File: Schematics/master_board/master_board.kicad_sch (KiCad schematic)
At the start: 48 parts, among them J1 2x5x1.27mm, J2 USB_C_Receptacle_USB2.0, J3 Conn_01x01_Female, J4 Conn_01x01_Female, J5 Conn_01x01_Female, J6 Conn_01x01_Female, SW1 SW_Push, SW2 SW_Push, SW3 SW_Push, U1 NCP1117-3.3_SOT223, U2 RP2040, U3 W25Q16JVSSIQ, Y1 ABLS-12.000MHZ-B4-T

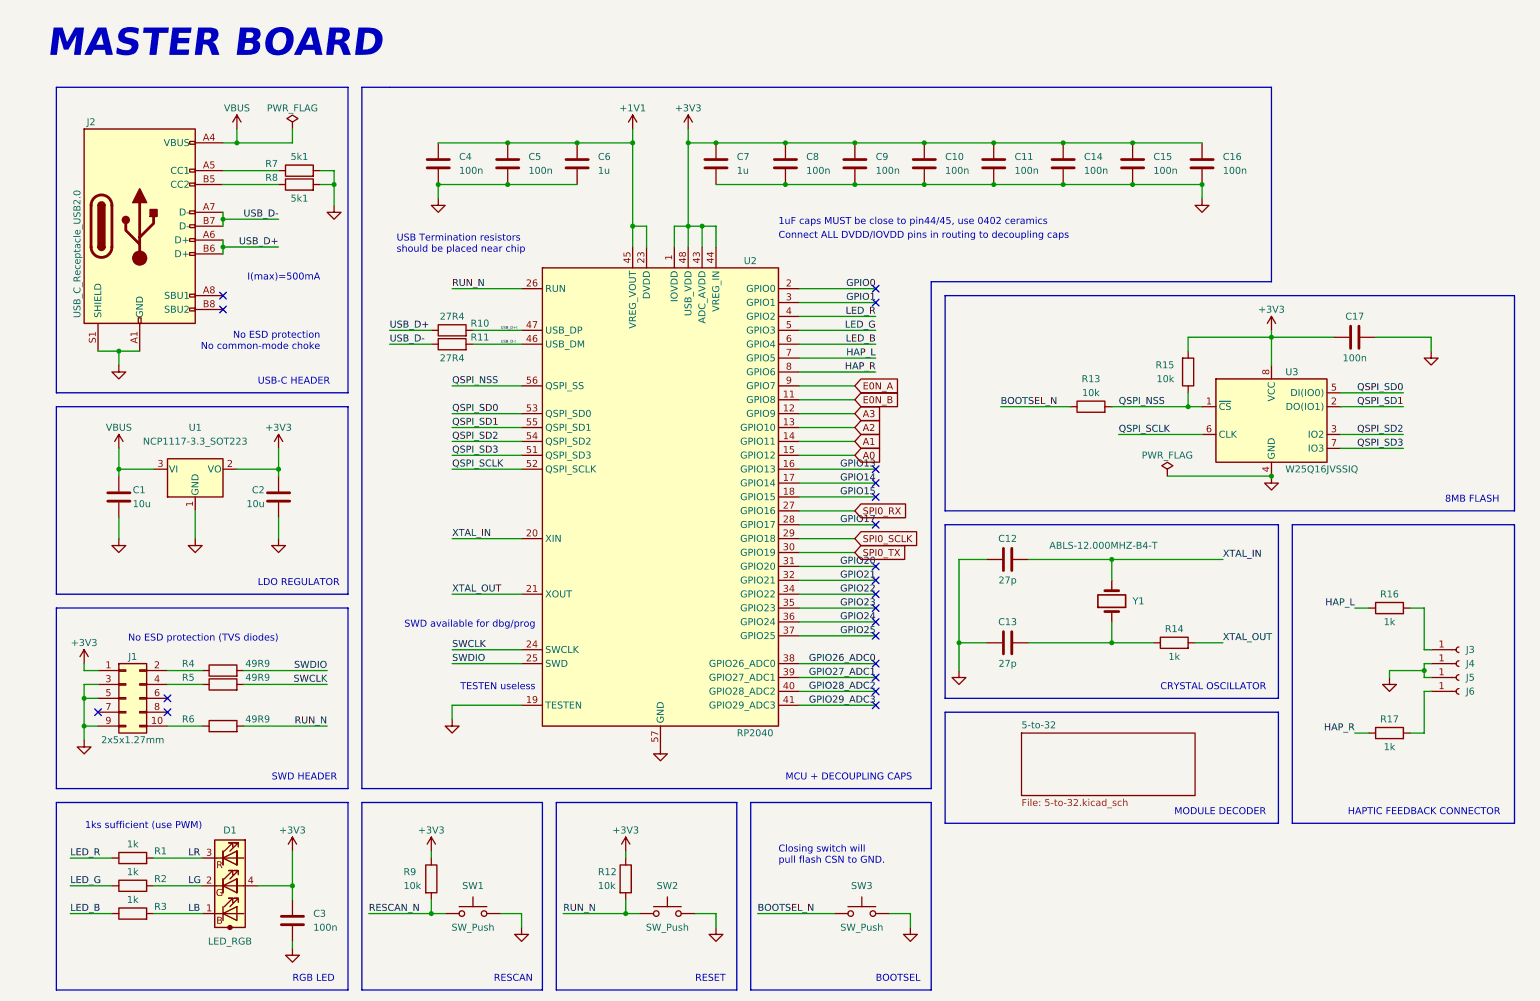
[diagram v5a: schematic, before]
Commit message: Finalize master board placement, begin routing
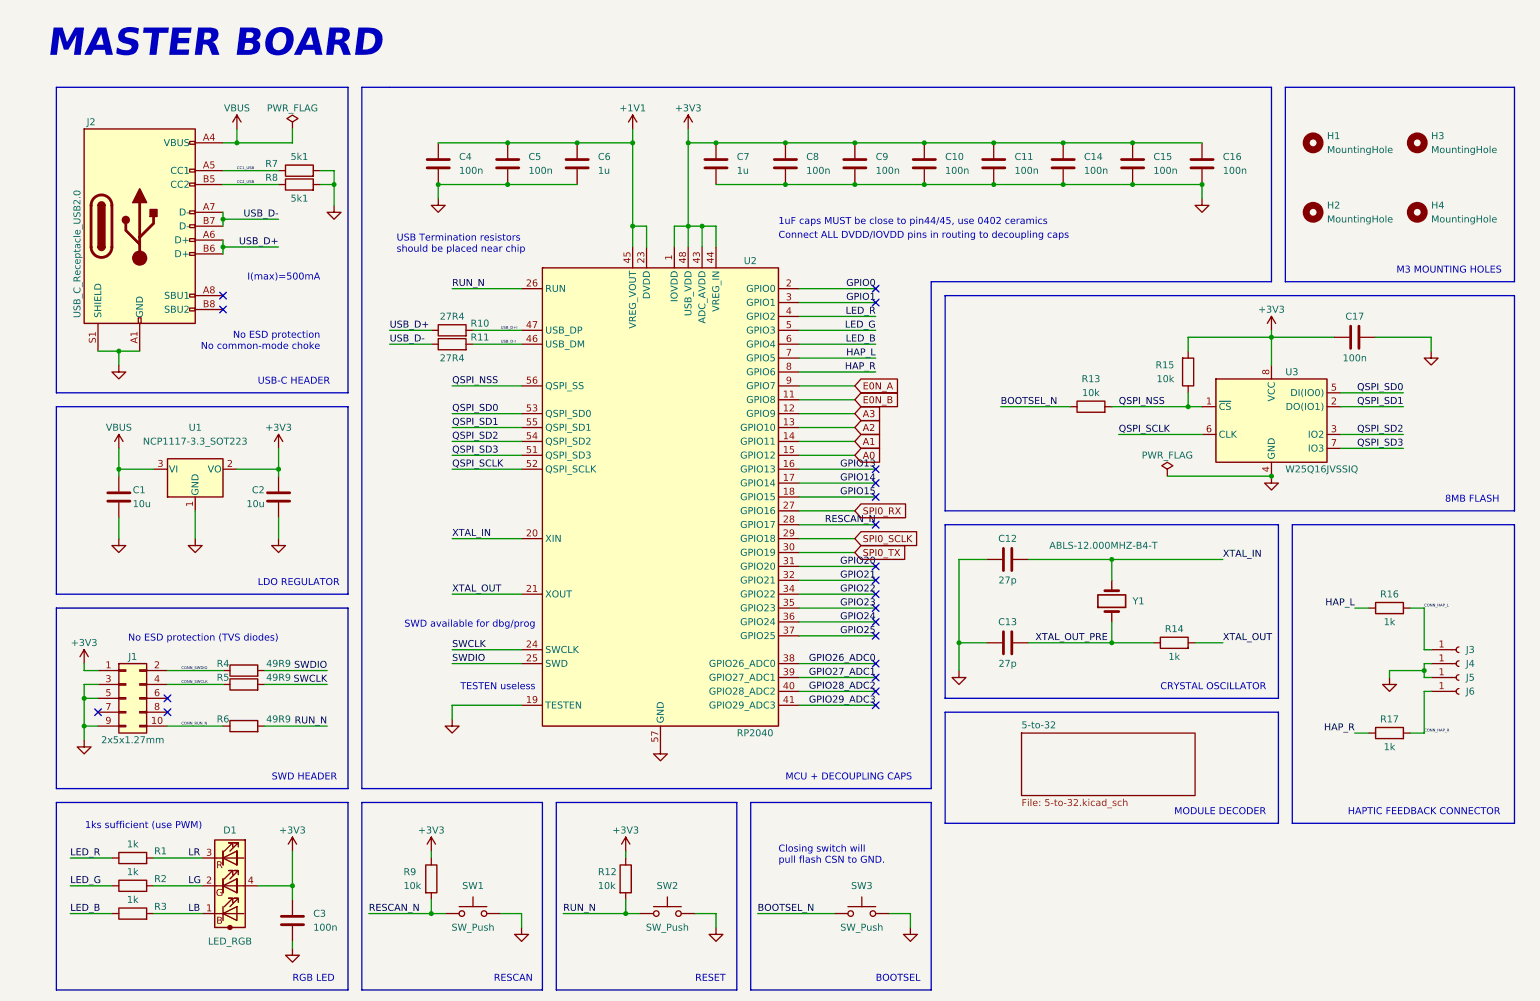
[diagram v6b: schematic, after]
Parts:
- added H1, H2, H3, H4: MountingHole, MountingHole:MountingHole_3.2mm_M3, symbol Mechanical:MountingHole
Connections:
- net GPIO17 is gone; now on net RESCAN_N: U2.28 (GPIO17)
- net CONN_RUN_N: now reaches J1.10 (Pin_10), R6.1
- net CONN_SWDIO: now reaches J1.2 (Pin_2), R4.1
- net CONN_SWCLK: now reaches J1.4 (Pin_4), R5.1
- net CONN_HAP_L: now reaches J3.1 (Pin_1), R16.2
- net XTAL_OUT_PRE: now reaches C13.2, R14.1, Y1.1
- net CC1_USB: now reaches J2.A5 (CC1), R7.1
- net CONN_HAP_R: now reaches J6.1 (Pin_1), R17.2
- net CC2_USB: now reaches J2.B5 (CC2), R8.1
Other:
- note added: "M3 MOUNTING HOLES"
- moved on the sheet: R4, R5, R6

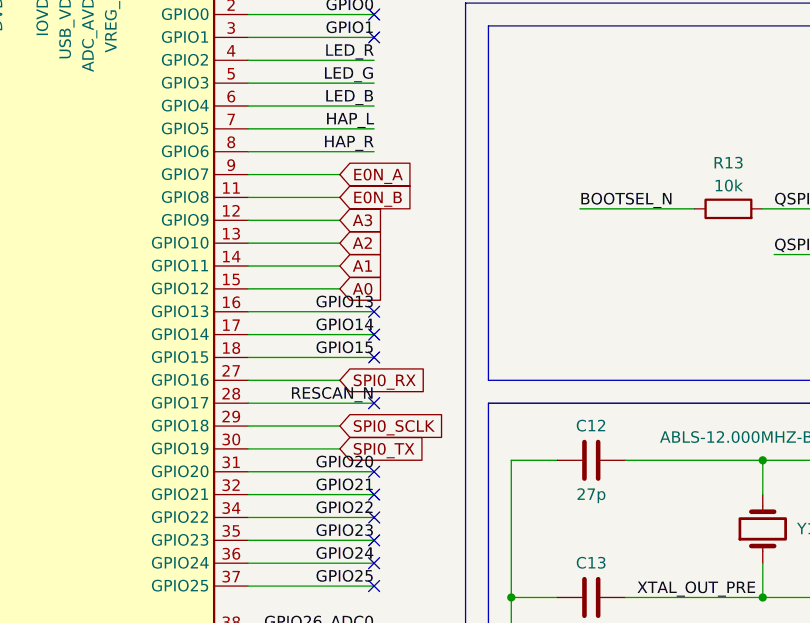
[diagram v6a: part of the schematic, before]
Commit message: Route master board and DRC
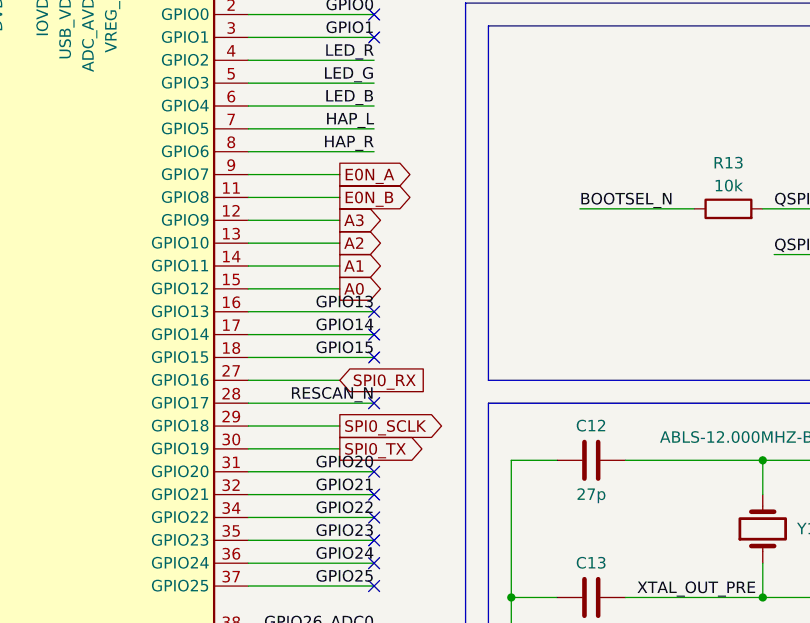
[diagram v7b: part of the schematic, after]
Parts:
- C1, C2: footprint Capacitor_SMD:C_0402_1005Metric -> Capacitor_SMD:C_0805_2012Metric
- R1, R10, R11, R12, R13, R14, R15, R16, R17, R2, R3, R4, R5, R6, R7, R8, R9: footprint Resistor_SMD:R_01005_0402Metric -> Resistor_SMD:R_0402_1005Metric

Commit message: Master board finishing touches
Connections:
- net HAP_L: now also U2.8 (GPIO6); no longer U2.7 (GPIO5)
- net HAP_R: now also U2.7 (GPIO5); no longer U2.8 (GPIO6)
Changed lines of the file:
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@@
     (effects (font (size 5 5) (thickness 1) bold italic) (justify right bottom))
   )
-  (label "HAP_R" (at 165.1 81.28 180)
+  (label "HAP_L" (at 165.1 81.28 180)
     (effects (font (size 1.27 1.27)) (justify right bottom))
   )
@@
   (label "XTAL_OUT_PRE" (at 194.31 130.81 0)
     (effects (font (size 1.27 1.27)) (justify left bottom))
-  )
-  (label "HAP_L" (at 165.1 78.74 180)
-    (effects (font (size 1.27 1.27)) (justify right bottom))
   )
   (label "CONN_RUN_N" (at 38.1 146.05 0)
@@
     (effects (font (size 1.27 1.27)) (justify left bottom))
   )
+  (label "HAP_R" (at 165.1 78.74 180)
+    (effects (font (size 1.27 1.27)) (justify right bottom))
+  )
   (label "SWCLK" (at 64.77 138.43 180)
